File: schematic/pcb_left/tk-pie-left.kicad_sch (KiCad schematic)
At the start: 29 parts, among them J2 DBG

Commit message: Remove interloping extra button
Don't know why they were there but now they are dead and no-one will be
the wiser...
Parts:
- removed S20: MX_SW_SOCKET_RGB_REV, Footprints:MX_SW_SOCKET_LED_REV, symbol library:MX_SW_SOCKET_RGB_REV
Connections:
- net S23 is gone; now on net S22: E6.1 (Pin_1)
- net S20: now also E4.1 (Pin_1)
- net S21: now also E5.1 (Pin_1); no longer E4.1 (Pin_1)
- net S22: no longer E5.1 (Pin_1)
- net at S19.6 (DOUT): now also E3.1 (Pin_1)

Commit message: Merge with hulthe schematics schenanigans
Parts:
- added C1, C2: C, symbol Device:C
- added C3: C_Polarized, symbol Device:C_Polarized_US
- added C4, C5: 12µF, symbol Device:C
- added D1: SS14, Diode_SMD:D_SMA, symbol Diode:SS14
- added L1: L, symbol Device:L
- added L2: 22µH, symbol Device:L
- added PS1: ME2108A33P, ME2108A33P:CONV_ME2108A33P, symbol library:ME2108A33P
- added R1, R2, R3, R4, R5: R, symbol Device:R
- added U2: TPS61027DRCR, DRC0010J, symbol library:TPS61027DRCR
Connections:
- net +5V: now also C4.2, C5.1, D1.1 (K), PS1.2 (VOUT)
- net GND: now also C1.2, C2.2, C3.2, C4.1, C5.2, PS1.3 (LX), R2.2, R4.1, U2.10 (PGND), U2.11 (PAD), U2.5 (GND), U2.8 (PS)
- new net: D1.2 (A), L2.2, PS1.1 (VSS)
- new net: C1.1, R1.1, U2.1 (EN), U2.6 (VBAT)
- new net: C2.1, C3.1, R3.1, R5.1, U2.2 (VOUT)
- new net: R3.2, R4.2, U2.3 (FB)
- new net: R5.2, U2.4 (LBO)
- new net: R1.2, R2.1, U2.7 (LBI)
- new net: L1.2, U2.9 (SW)
- new net Vbat: L2.1

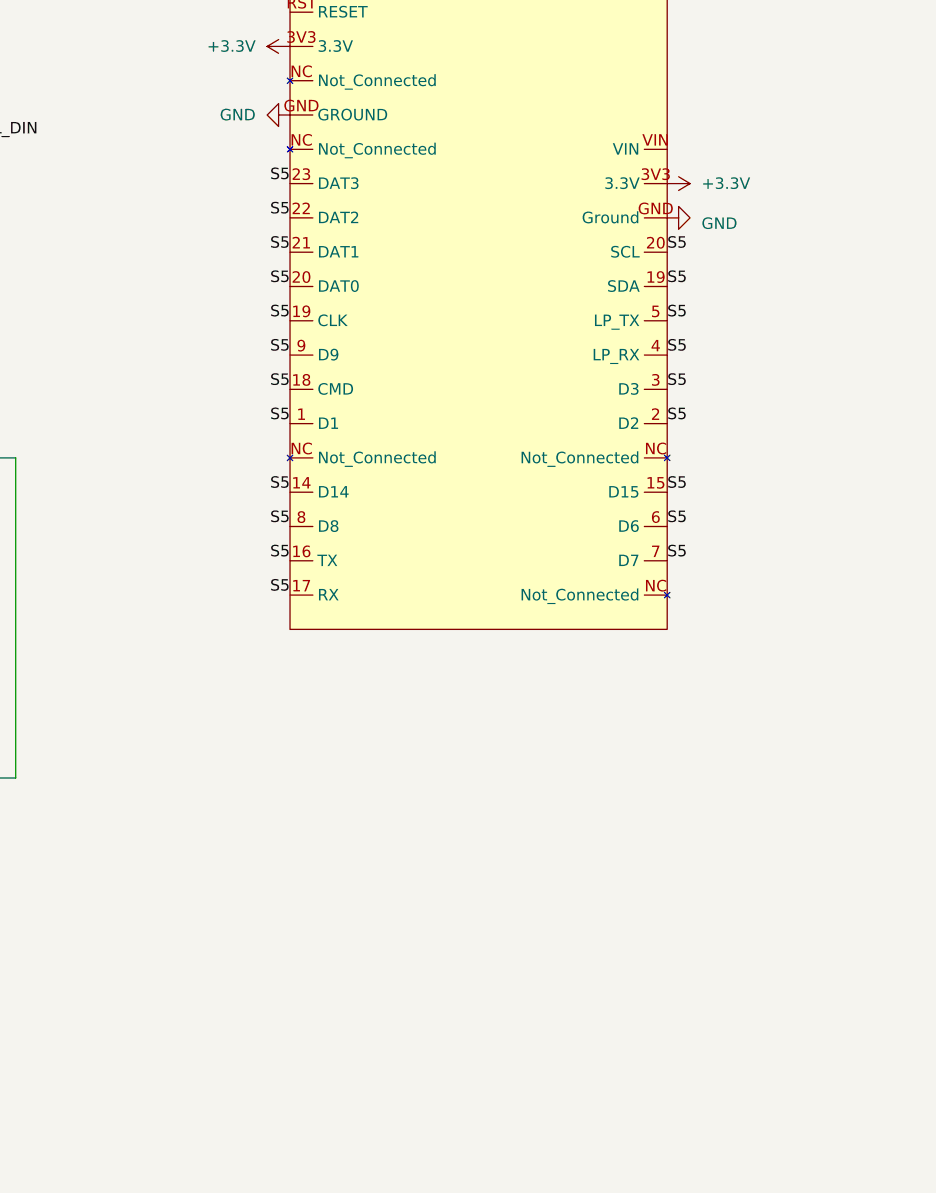
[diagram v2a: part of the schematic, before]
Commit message: Began assigning pins for left PCB
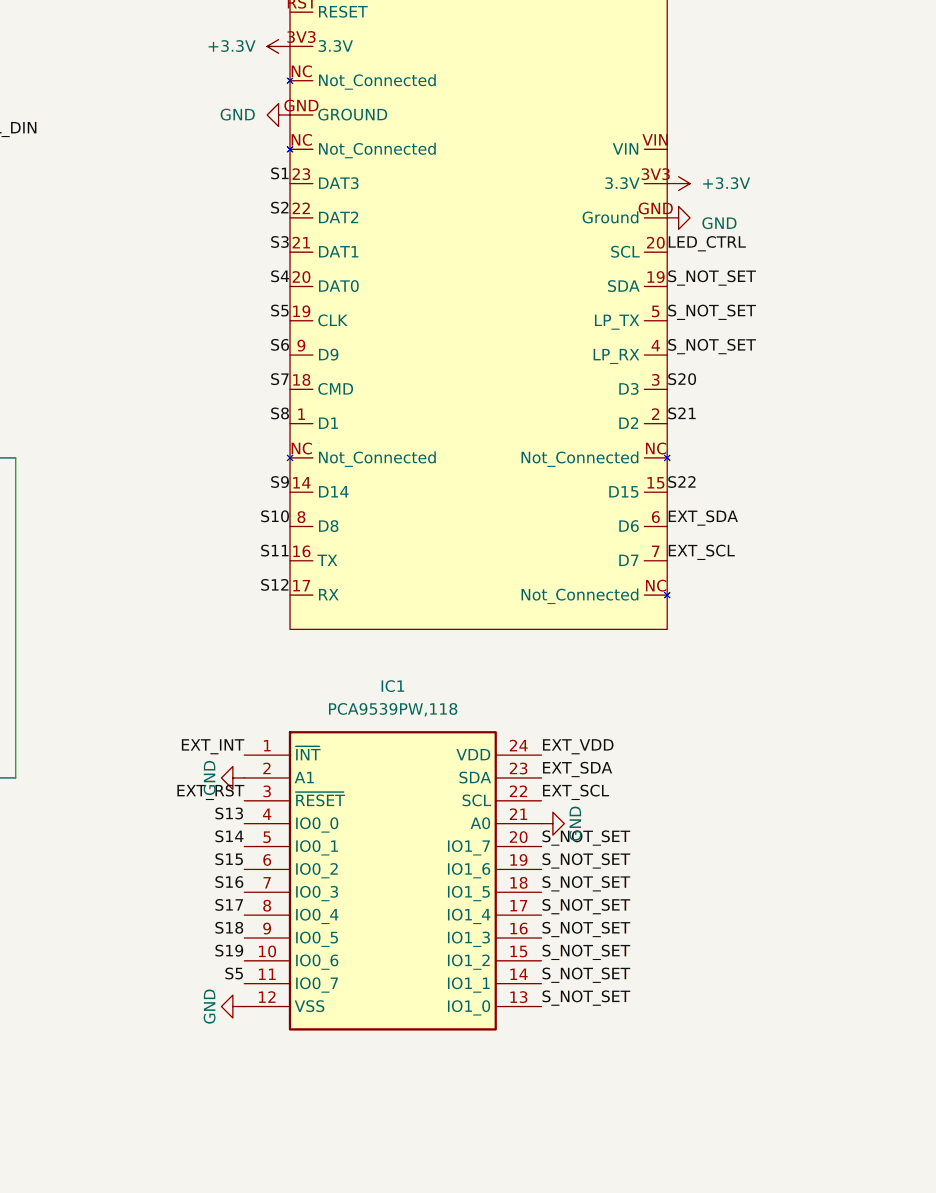
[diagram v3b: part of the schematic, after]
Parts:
- added IC1: PCA9539PW,118, SOP65P640X110-24N, symbol library:PCA9539PW,118
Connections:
- net GND: now also IC1.12 (VSS), IC1.2 (A1), IC1.21 (A0)
- net S1: now also U1.23 (DAT3)
- net S10: now also U1.8 (D8)
- net S11: now also U1.16 (TX)
- net S12: now also U1.17 (RX)
- net S13: now also IC1.4 (IO0_0)
- net S14: now also IC1.5 (IO0_1)
- net S15: now also IC1.6 (IO0_2)
- net S16: now also IC1.7 (IO0_3)
- net S17: now also IC1.8 (IO0_4)
- net S18: now also IC1.9 (IO0_5)
- net S19: now also IC1.10 (IO0_6)
- net S2: now also U1.22 (DAT2)
- net S20: now also U1.3 (D3)
- net S21: now also U1.2 (D2)
- net S22: now also U1.15 (D15)
- net S3: now also U1.21 (DAT1)
- net S4: now also U1.20 (SCL)
- net S5: now also IC1.11 (IO0_7); no longer U1.1 (D1), U1.14 (D14), U1.15 (D15), U1.16 (TX), U1.17 (RX), U1.18 (CMD), U1.2 (D2), U1.20 (SCL), U1.21 (DAT1), U1.22 (DAT2), U1.23 (DAT3), U1.3 (D3), U1.4 (LP_RX), U1.5 (LP_TX), U1.6 (D6), U1.7 (D7), U1.8 (D8), U1.9 (D9)
- net S6: now also U1.9 (D9)
- net S7: now also U1.18 (CMD)
- net S8: now also U1.1 (D1)
- net S9: now also U1.14 (D14)
- new net EXT_INT: IC1.1 (~{INT})
- new net EXT_RST: IC1.3 (~{RESET})
- new net EXT_SCL: IC1.22 (SCL), U1.7 (D7)
- new net EXT_SDA: IC1.23 (SDA), U1.6 (D6)
- new net EXT_VDD: IC1.24 (VDD)
- new net LED_CTRL: U1.20 (SCL)
- new net S_NOT_SET: IC1.13 (IO1_0), IC1.14 (IO1_1), IC1.15 (IO1_2), IC1.16 (IO1_3), IC1.17 (IO1_4), IC1.18 (IO1_5), IC1.19 (IO1_6), IC1.20 (IO1_7), U1.19 (SDA), U1.4 (LP_RX), U1.5 (LP_TX)

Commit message: Update schematic
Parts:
- removed J2: DBG, Connector_PinSocket_2.54mm:PinSocket_1x03_P2.54mm_Vertical, symbol Connector:Conn_01x03_Pin
- removed MCU1: ITSYBITSY RP2040, Footprints:ITSYBITSY BREAKOUT, symbol library:ITSYBITSY_RP2040

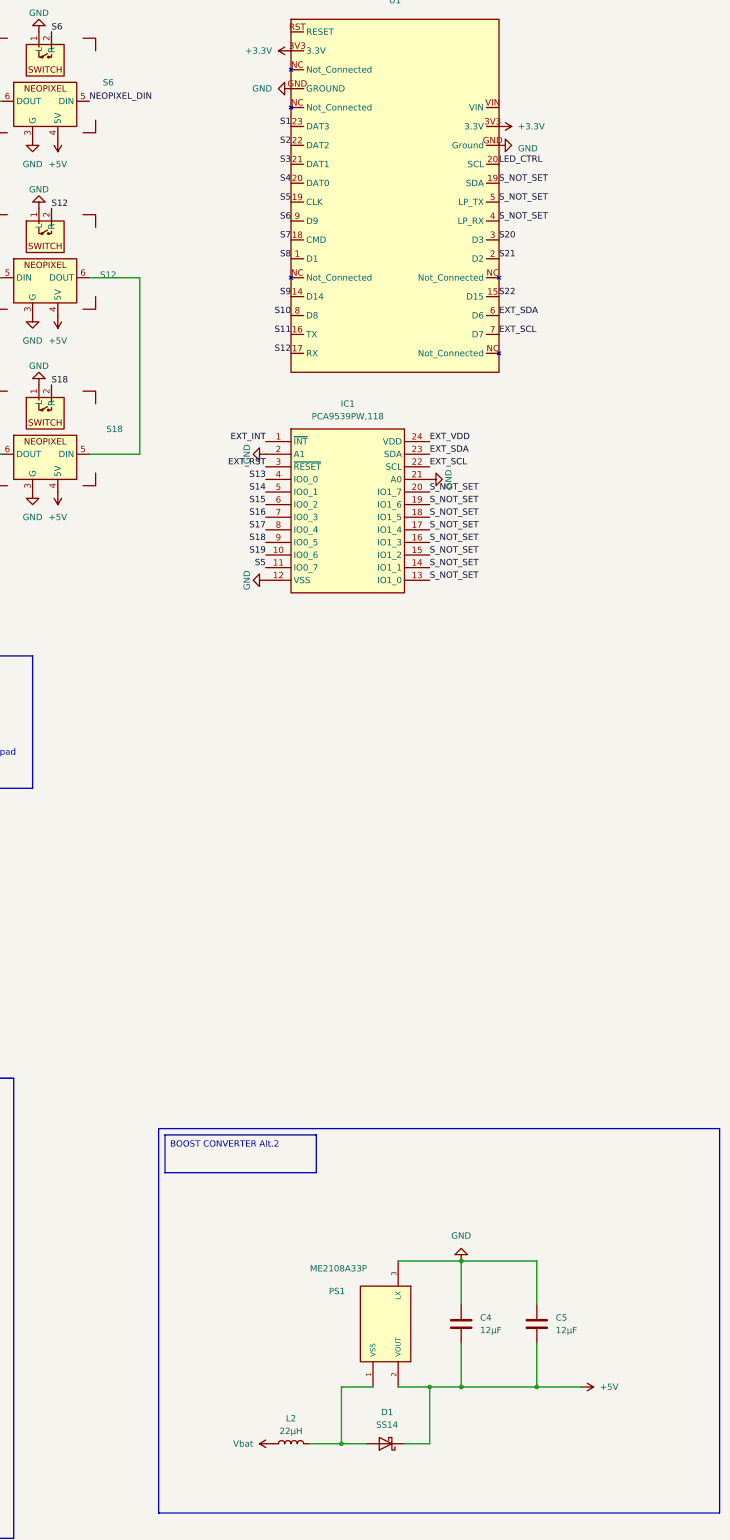
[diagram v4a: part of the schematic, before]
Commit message: Update/fix ME2108 schematic
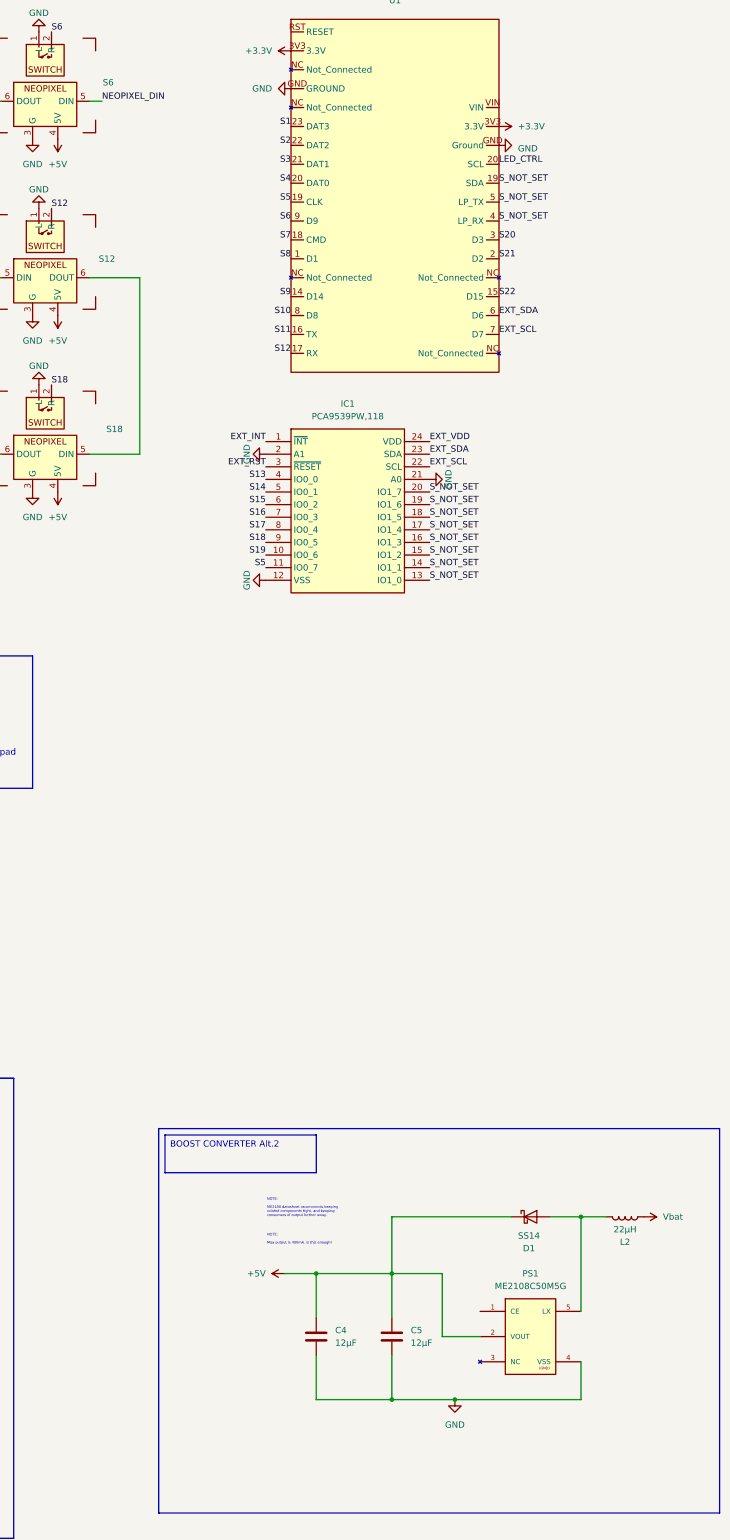
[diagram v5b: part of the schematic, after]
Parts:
- removed PS1: ME2108A33P, ME2108A33P:CONV_ME2108A33P, symbol library:ME2108A33P
- added PS1: ME2108C50M5G, Package_TO_SOT_SMD:SOT-23-5, symbol library:ME2108C50M5G
- U1: footprint KeyboardFootprints:DFR1075 -> Footprints:DFR1075
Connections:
- net +5V: now also C4.1, C5.2, PS1.2 (VOUT); no longer C4.2, C5.1
- net GND: now also C4.2, C5.1, PS1.4 (VSS); no longer C4.1, C5.2
- net at D1.2 (A), L2.2: now also PS1.5 (LX)
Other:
- note added: "NOTE: ME2108 datasheet recommends keeping related components tight, and keeping consumers of output further away."
- note added: "NOTE: Max output is 400mA. is this enough?"
- moved on the sheet: C4, C5, D1, L2
